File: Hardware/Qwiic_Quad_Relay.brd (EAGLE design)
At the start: 82.5 x 47 mm, 122 parts, among them J2 Qwiic Right Angle, J3 Qwiic Right Angle, J4 AVR_SPI_PROG_3X2TESTPOINTS, J9 POWER_JACK, K1 RELAY-SPDT-JZC-11F, K2 RELAY-SPDT-JZC-11F, K3 RELAY-SPDT-JZC-11F, K4 RELAY-SPDT-JZC-11F, Q1 600mA/40V, Q2 600mA/40V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

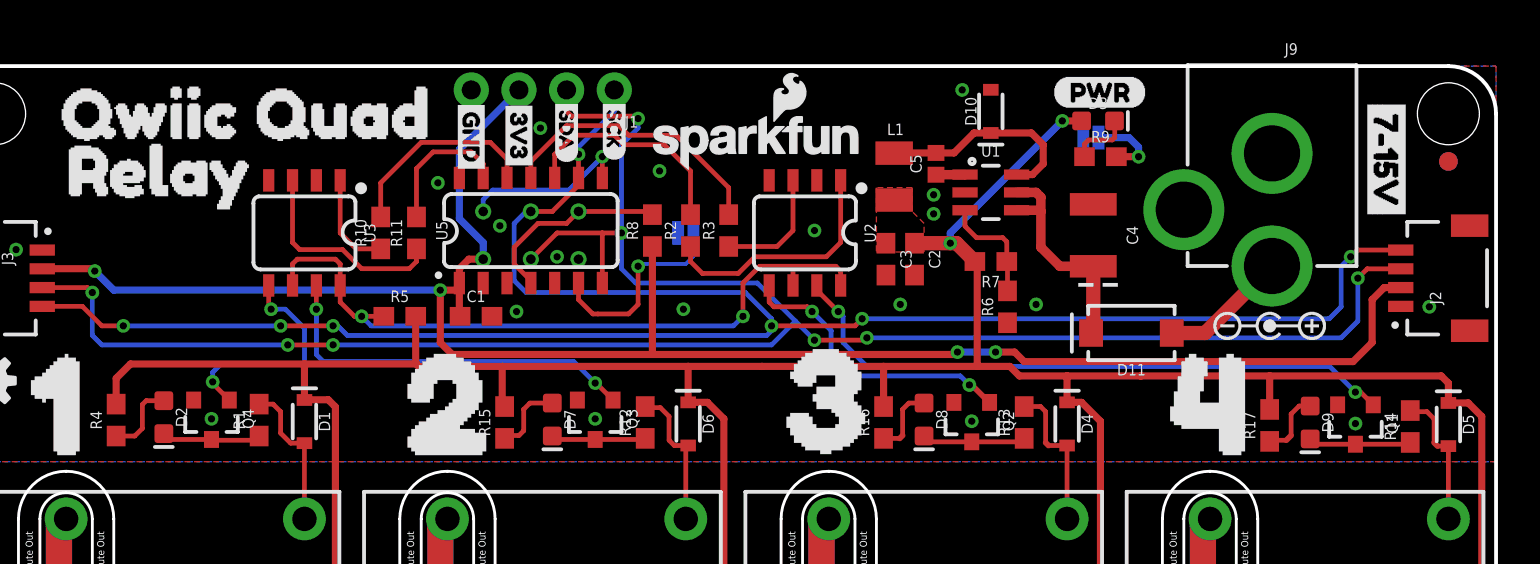
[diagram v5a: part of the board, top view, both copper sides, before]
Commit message: Fixes various minor DRC issues
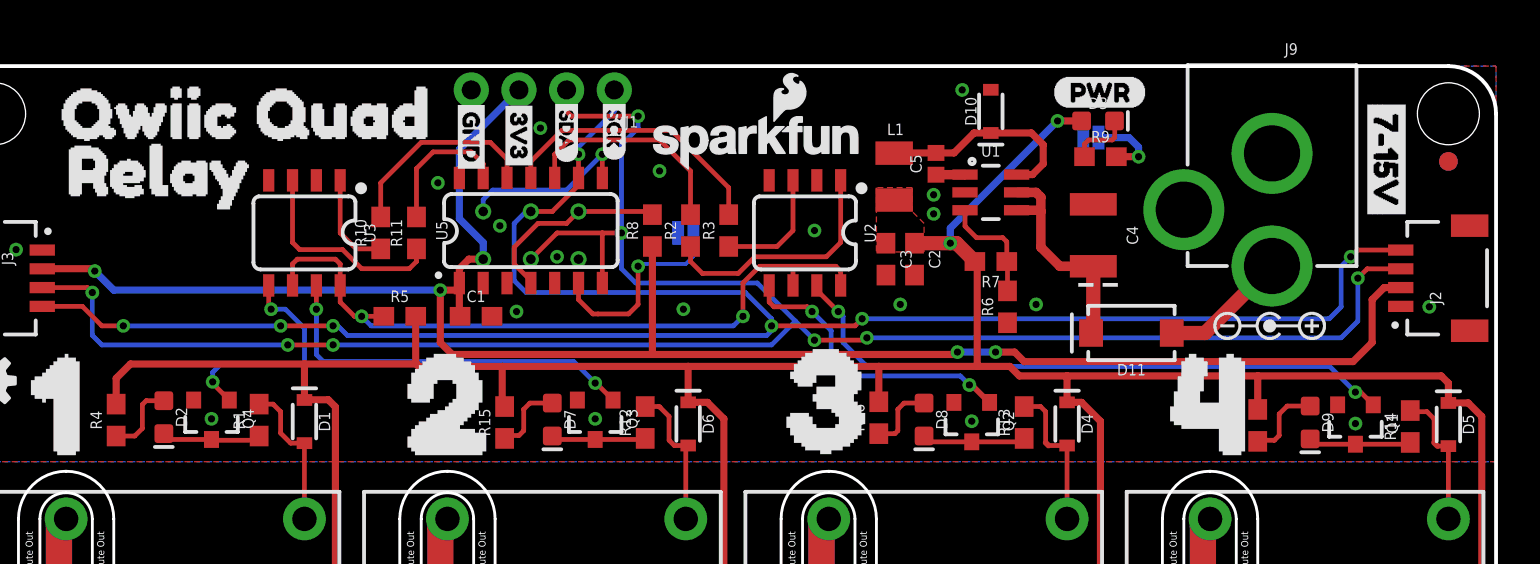
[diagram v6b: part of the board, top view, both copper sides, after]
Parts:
- moved R17 0.64 mm to (69.8, 27.8)
- moved R16 0.36 mm to (49.7, 28.3)
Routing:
- net N$8: track 3.61 -> 4.24 mm

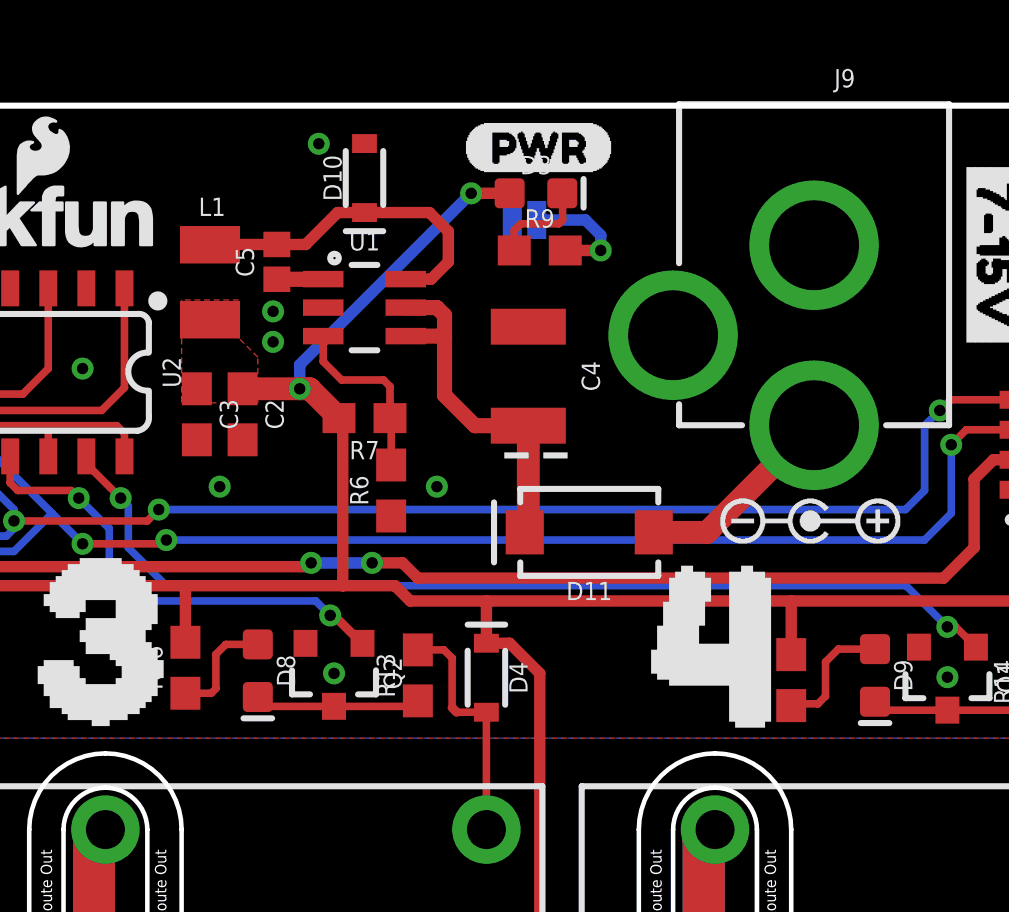
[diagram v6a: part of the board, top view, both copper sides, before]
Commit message: Adds polygons for switch pin and VIN
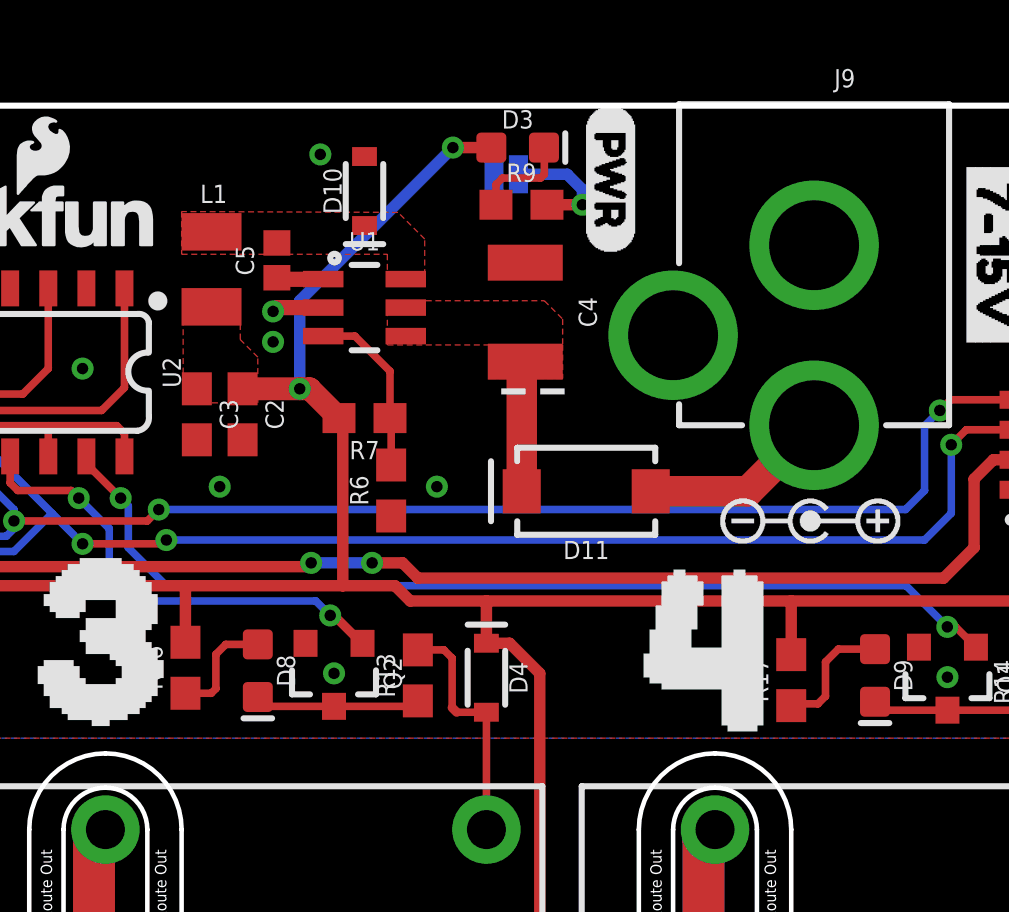
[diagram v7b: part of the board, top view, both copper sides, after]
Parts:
- moved U$1 5.11 mm to (63.8, 47.0), turned to 270 degrees
- moved C4 2.14 mm to (61.0, 40.1)
- moved D3 1.64 mm to (60.7, 45.6)
- moved LED 1.64 mm to (60.4, 44.7)
- moved R9 1.64 mm to (60.9, 43.7)
- moved D11 1.38 mm to (63.0, 34.1)
- moved L1 0.43 mm to (50.6, 41.6)
- moved D10 0.43 mm to (55.6, 44.1)
- moved U$5 0.28 mm to (60.3, 28.8)
- moved C5 0.05 mm to (52.7, 41.8)
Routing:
- net SW: track 11.3 -> 0.01 mm
- net VIN_DC_DC: track 12.2 -> 4.39 mm
- net GND: track 0.00 -> 1.73 mm
- net 5V: track 171.0 -> 172.3 mm
- added copper zone on layer 1, net SW
- added copper zone on layer 1, net VIN_DC_DC

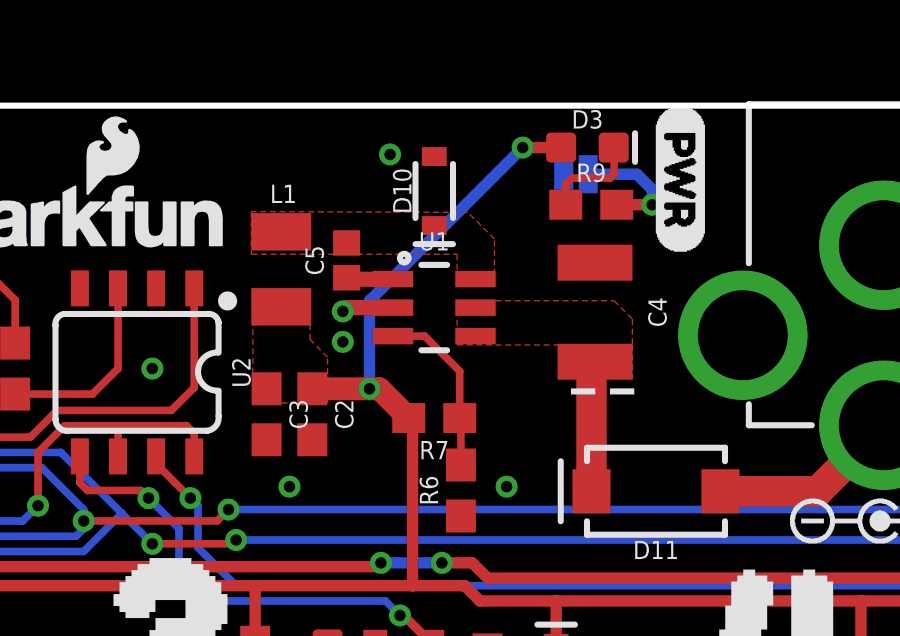
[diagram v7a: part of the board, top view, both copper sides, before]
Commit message: Updates inductor with inductor with correct amperage rating
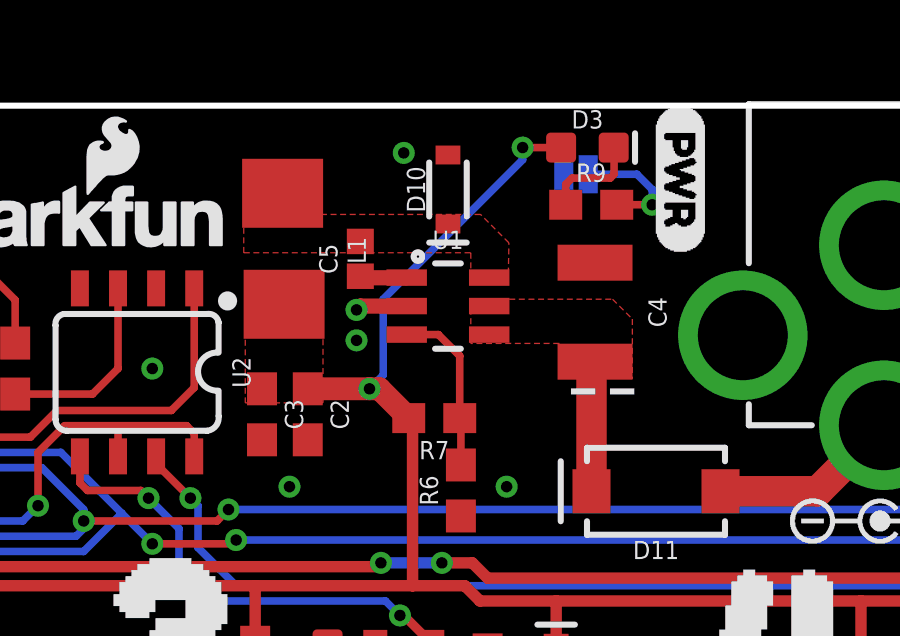
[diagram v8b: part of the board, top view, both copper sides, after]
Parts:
- L1: device SparkFun-Coils:INDUCTOR_LQH32 -> SparkFun-Coils:INDUCTOR_15UH
- moved L1 0.58 mm to (50.6, 42.2), turned to 270 degrees
- moved C5 0.46 mm to (53.2, 41.9)
- moved U1 0.46 mm to (56.1, 40.3)
- moved D10 0.46 mm to (56.1, 44.2)
- moved C2 0.15 mm to (51.4, 36.7)
- moved C3 0.15 mm to (49.9, 36.7)
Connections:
- net 5V: now also L1.P2; no longer L1.P$2
- net SW: now also L1.P1; no longer L1.P$1
